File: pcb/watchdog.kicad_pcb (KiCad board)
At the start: 2 copper layers, 21.8 x 14.6 mm, 5 parts, among them J1 Conn_01x05_Male, J2 AVR-ISP-6, U1 ATtiny45-20PU

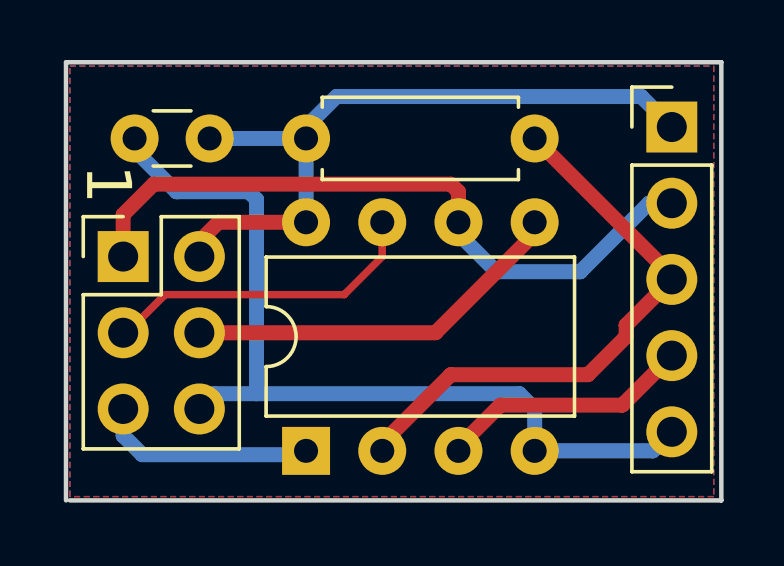
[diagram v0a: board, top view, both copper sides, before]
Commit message: watchdog.py, pulse variant: Fore a minimal watch time
Otherwise, a start() signal looks like a stop() signal.

Also: Minor change on the PCB. Add a label and make the board
just a little bit smaller by narrowing the edges.
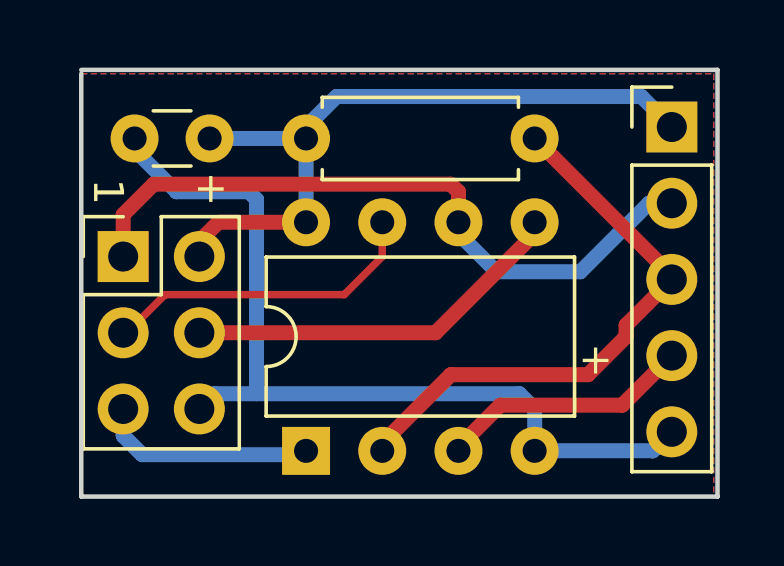
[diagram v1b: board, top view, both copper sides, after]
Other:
- board size 21.8 x 14.6 mm -> 21.2 x 14.2 mm
- board text added: "+"
- board text added: "Sts"
- board text removed: "Log"
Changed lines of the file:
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@@
   (general
     (thickness 1.6)
-    (drawings 10)
+    (drawings 12)
     (tracks 54)
     (zones 0)
@@
     )
   )
-  (gr_text 1 (at 96.774 73.914 270) (layer F.SilkS)
-    (effects (font (size 1.5 1.5) (thickness 0.3)))
-  )
-  (gr_line (start 95.377 69.85) (end 117.221 69.85) (angle 90) (layer Edge.Cuts) (width 0.15))
-  (gr_line (start 95.504 84.455) (end 117.221 84.455) (angle 90) (layer Edge.Cuts) (width 0.15))
+  (gr_line (start 95.885 70.231) (end 95.885 84.328) (angle 90) (layer Edge.Cuts) (width 0.15))
+  (gr_line (start 117.094 70.104) (end 117.094 84.328) (angle 90) (layer Edge.Cuts) (width 0.15))
+  (gr_line (start 95.885 84.328) (end 117.094 84.328) (angle 90) (layer Edge.Cuts) (width 0.15))
+  (gr_line (start 95.885 70.104) (end 117.094 70.104) (angle 90) (layer Edge.Cuts) (width 0.15))
+  (gr_text + (at 100.203 74.041) (layer F.SilkS)
+    (effects (font (size 1 1) (thickness 0.2)))
+  )
+  (gr_text + (at 113.03 79.756) (layer F.SilkS)
+    (effects (font (size 1 1) (thickness 0.2)))
+  )
+  (gr_text 1 (at 96.774 74.168 270) (layer F.SilkS)
+    (effects (font (size 1 1) (thickness 0.2)))
+  )
   (gr_text Reset (at 114.427 79.502) (layer B.SilkS)
     (effects (font (size 1 1) (thickness 0.2)) (justify left mirror))
@@
     (effects (font (size 1 1) (thickness 0.2)) (justify mirror))
   )
-  (gr_text Log (at 113.03 74.549) (layer B.SilkS)
+  (gr_text Sts (at 113.03 74.549) (layer B.SilkS)
     (effects (font (size 1 1) (thickness 0.2)) (justify mirror))
   )
@@
     (effects (font (size 1 1) (thickness 0.2)) (justify mirror))
   )
-  (gr_line (start 95.377 84.455) (end 95.377 69.85) (angle 90) (layer Edge.Cuts) (width 0.15))
-  (gr_line (start 117.221 69.85) (end 117.221 84.455) (angle 90) (layer Edge.Cuts) (width 0.15))
   (segment (start 110.998 82.804) (end 114.935 82.804) (width 0.5) (layer B.Cu) (net 1) (status C00000))
   (segment (start 114.935 82.804) (end 115.57 82.169) (width 0.5) (layer B.Cu) (net 1) (status C00000))
@@
     (polygon
       (pts
-        (xy 116.967 84.328) (xy 95.504 84.328) (xy 95.504 69.977) (xy 116.967 69.977)
+        (xy 116.967 84.328) (xy 95.885 84.328) (xy 95.885 70.231) (xy 116.967 70.231)
       )
     )
@@
     (polygon
       (pts
-        (xy 116.967 84.328) (xy 95.504 84.328) (xy 95.504 69.977) (xy 116.967 69.977)
+        (xy 116.967 84.328) (xy 95.885 84.328) (xy 95.885 70.231) (xy 116.967 70.231)
       )
     )

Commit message: pcb: Change layout.
Rotate Attiny by 90°
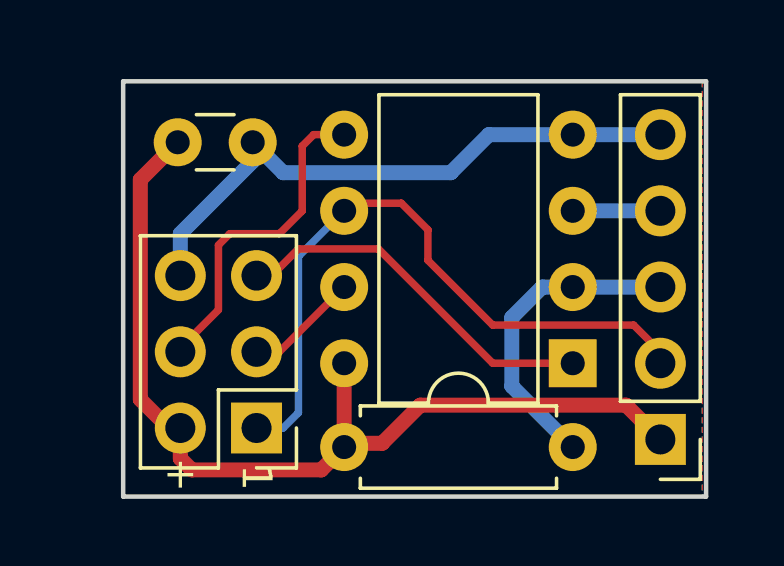
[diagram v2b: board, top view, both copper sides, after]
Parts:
- moved J1 10.4 mm to (115.2, 82.4), turned to 180 degrees
- moved R1 10.4 mm to (104.6, 82.7)
- moved U1 9.36 mm to (112.3, 79.9), turned to 180 degrees
- moved J2 7.24 mm to (101.7, 82.0), turned to 180 degrees
- moved C1 3.94 mm to (101.6, 72.5), turned to 180 degrees
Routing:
- net GND: track 29.4 -> 20.0 mm
- net Net-(C1-Pad2): track 23.8 -> 32.4 mm
- net Net-(J1-Pad3): track 19.0 -> 10.5 mm
- net Net-(J2-Pad3): track 10.8 -> 3.82 mm
- net Net-(J1-Pad4): track 8.50 -> 2.92 mm
- net Net-(J2-Pad5): track 7.25 -> 12.5 mm
- net Net-(J2-Pad4): track 12.9 -> 11.1 mm
- net Net-(J1-Pad2): track 23.1 -> 22.5 mm
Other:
- board size 21.2 x 14.2 mm -> 19.4 x 13.8 mm
- board text added: "F"
- board text added: "G"
- board text added: "R"
- board text added: "S"
- board text removed: "Feed"
- board text removed: "GND"
- board text removed: "Reset"
- board text removed: "Sts"
- board text removed: "Vcc"
